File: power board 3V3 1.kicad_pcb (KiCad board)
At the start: 2 copper layers, 63 x 36 mm, 29 parts, among them J1 UVLO TP, J2 CHRGR TP, J3 BATT & RPP TP, J4 LDO TP, J5 SRC CTRL TP, Q1 NMOS - HL3400A, Q2 PMOS - SI2301, Q3 PMOS - SI2301, U1 TP4056-42-ESOP8, U2 HT7533-1-SOT89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

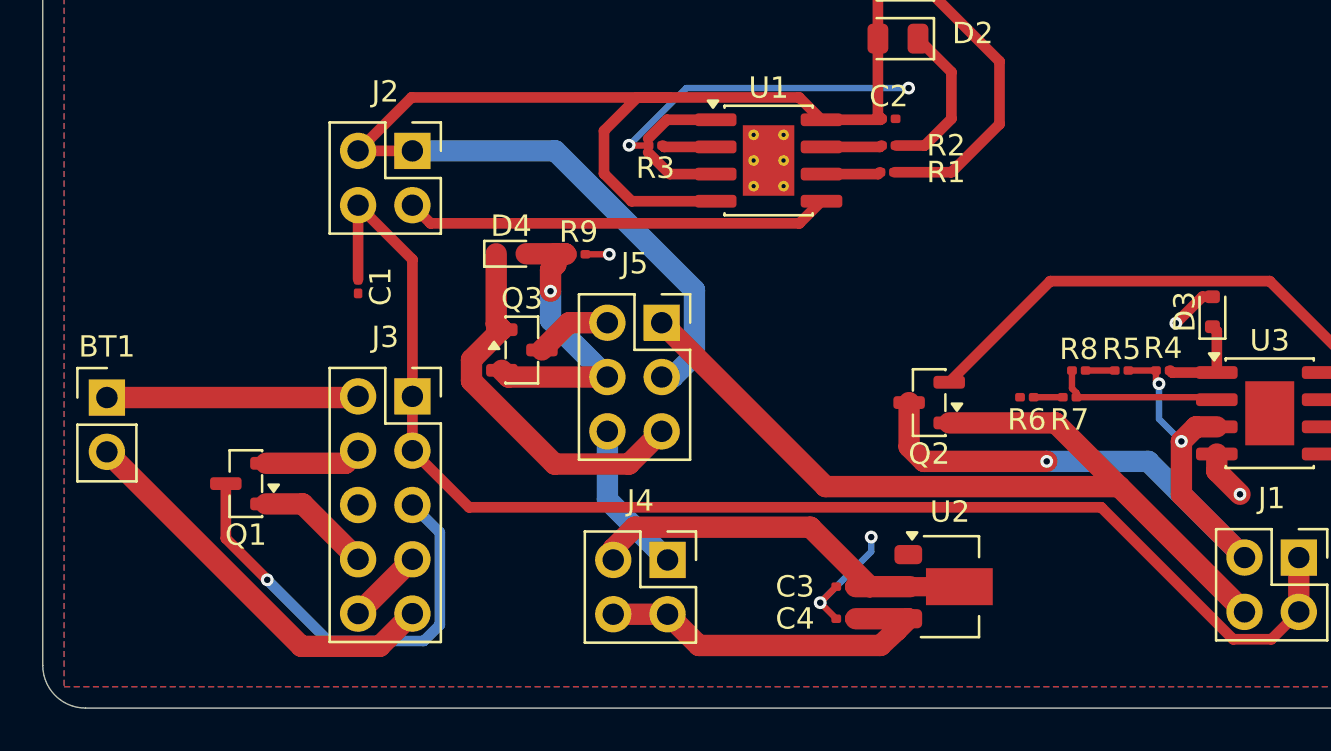
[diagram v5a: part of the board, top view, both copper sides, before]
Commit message: Labels done
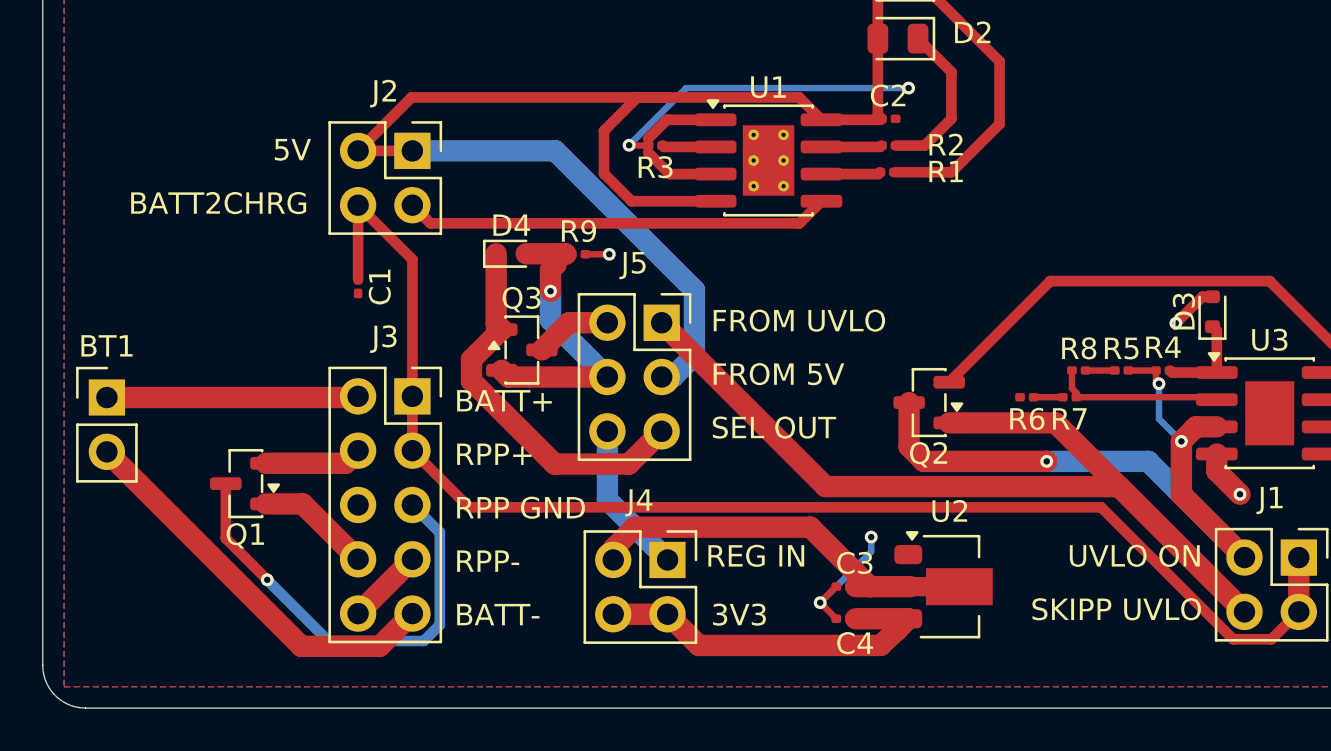
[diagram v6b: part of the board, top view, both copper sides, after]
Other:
- board text added: "3V3"
- board text added: "5V"
- board text added: "BATT+"
- board text added: "BATT-"
- board text added: "BATT2CHRG"
- board text added: "FROM 5V"
- board text added: "FROM UVLO"
- board text added: "REG IN"
- board text added: "RPP GND"
- board text added: "RPP+"
- board text added: "RPP-"
- board text added: "SEL OUT"
- board text added: "SKIPP UVLO"
- board text added: "UVLO ON"
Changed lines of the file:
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@@
 		(tags "capacitor")
 		(property "Reference" "C3"
-			(at 2.25 0 0)
+			(at -0.5655 1.0705 0)
 			(layer "F.SilkS")
 			(effects
@@
 		(tags "capacitor")
 		(property "Reference" "C4"
-			(at 2.25 0 0)
+			(at -0.5655 -1.1795 0)
 			(layer "F.SilkS")
 			(effects
@@
 		(layer "Edge.Cuts")
 	)
+	(gr_text "FROM UVLO"
+		(at 70.25 70.5 0)
+		(layer "F.SilkS")
+		(effects
+			(font
+				(size 1 1)
+				(thickness 0.15)
+			)
+			(justify left bottom)
+		)
+	)
+	(gr_text "BATT-"
+		(at 58.25 84.25 0)
+		(layer "F.SilkS")
+		(effects
+			(font
+				(size 1 1)
+				(thickness 0.15)
+			)
+			(justify left bottom)
+		)
+	)
+	(gr_text "RPP GND"
+		(at 58.25 79.25 0)
+		(layer "F.SilkS")
+		(effects
+			(font
+				(size 1 1)
+				(thickness 0.15)
+			)
+			(justify left bottom)
+		)
+	)
+	(gr_text "RPP-"
+		(at 58.25 81.75 0)
+		(layer "F.SilkS")
+		(effects
+			(font
+				(size 1 1)
+				(thickness 0.15)
+			)
+			(justify left bottom)
+		)
+	)
+	(gr_text "3V3"
+		(at 70.25 84.25 0)
+		(layer "F.SilkS")
+		(effects
+			(font
+				(size 1 1)
+				(thickness 0.15)
+			)
+			(justify left bottom)
+		)
+	)
+	(gr_text "UVLO ON"
+		(at 93.25 81.5 0)
+		(layer "F.SilkS")
+		(effects
+			(font
+				(size 1 1)
+				(thickness 0.15)
+			)
+			(justify right bottom)
+		)
+	)
+	(gr_text "REG IN"
+		(at 70 81.5 0)
+		(layer "F.SilkS")
+		(effects
+			(font
+				(size 1 1)
+				(thickness 0.15)
+			)
+			(justify left bottom)
+		)
+	)
+	(gr_text "RPP+"
+		(at 58.25 76.75 0)
+		(layer "F.SilkS")
+		(effects
+			(font
+				(size 1 1)
+				(thickness 0.15)
+			)
+			(justify left bottom)
+		)
+	)
+	(gr_text "SKIPP UVLO"
+		(at 93.25 84 0)
+		(layer "F.SilkS")
+		(effects
+			(font
+				(size 1 1)
+				(thickness 0.15)
+			)
+			(justify right bottom)
+		)
+	)
+	(gr_text "BATT2CHRG"
+		(at 43 65 0)
+		(layer "F.SilkS")
+		(effects
+			(font
+				(size 1 1)
+				(thickness 0.15)
+			)
+			(justify left bottom)
+		)
+	)
+	(gr_text "BATT+"
+		(at 58.25 74.25 0)
+		(layer "F.SilkS")
+		(effects
+			(font
+				(size 1 1)
+				(thickness 0.15)
+			)
+			(justify left bottom)
+		)
+	)
+	(gr_text "FROM 5V"
+		(at 70.25 73 0)
+		(layer "F.SilkS")
+		(effects
+			(font
+				(size 1 1)
+				(thickness 0.15)
+			)
+			(justify left bottom)
+		)
+	)
+	(gr_text "SEL OUT"
+		(at 70.25 75.5 0)
+		(layer "F.SilkS")
+		(effects
+			(font
+				(size 1 1)
+				(thickness 0.15)
+			)
+			(justify left bottom)
+		)
+	)
+	(gr_text "5V"
+		(at 49.75 62.5 0)
+		(layer "F.SilkS")
+		(effects
+			(font
+				(size 1 1)
+				(thickness 0.15)
+			)
+			(justify left bottom)
+		)
+	)
 	(segment

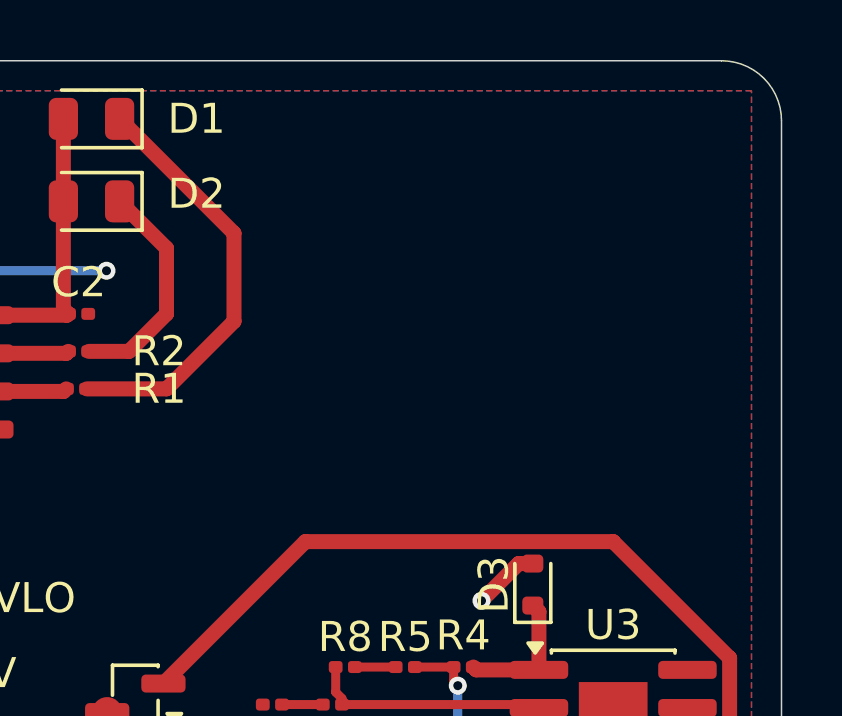
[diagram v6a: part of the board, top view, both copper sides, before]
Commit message: Added silkscreen github link
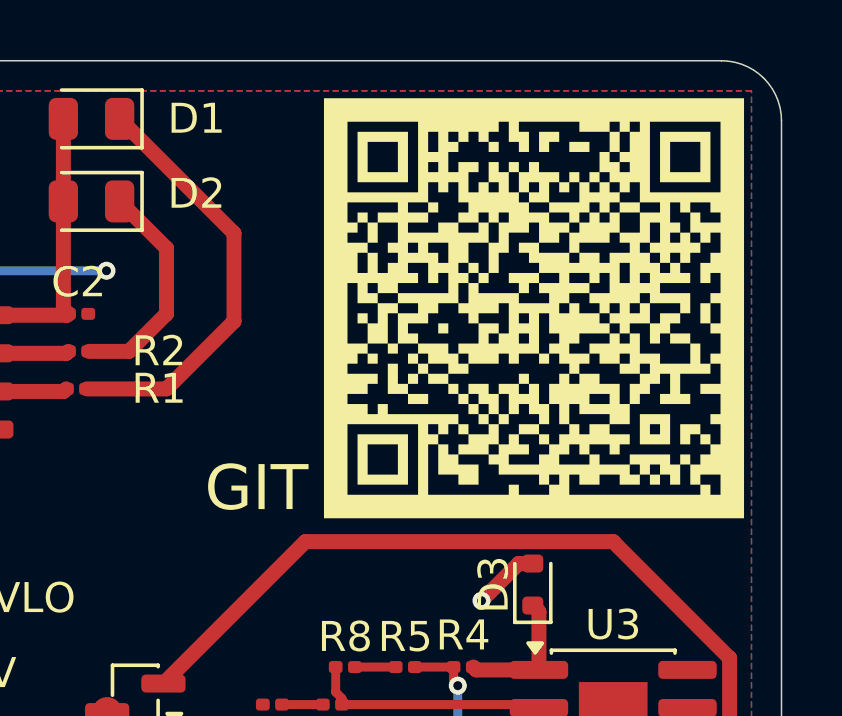
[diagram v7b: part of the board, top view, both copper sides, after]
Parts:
- added GIT: LOGO, LOGO, F.Cu at (93.8, 60.2)
